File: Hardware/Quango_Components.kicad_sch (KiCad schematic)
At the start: 112 parts, among them J1 Conn_01x12_Male, J2 Conn_01x12_Male, J3 Conn_01x12_Male, J4 Conn_01x12_Male, J5 SWD_Header, J6 Eurorack_10_pin_power, Q1 MMBT3904, U1 LM1117-3.3, U2 STM32G473V, U3 LM1117-5.0, U4 PS508, U5 MCP6002, U6 AS3364, U7 AS3364, U8 AD5676, U9 MCP48CMB21, Y1 8MHz 20pF

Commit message: Added Test Points
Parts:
- added TP1, TP2, TP3, TP4, TP5, TP6, TP7: TestPoint, Connector_PinSocket_2.54mm:PinSocket_1x01_P2.54mm_Vertical, symbol Connector:TestPoint
- D2, D3: symbol Diode:1N5819 -> Device:D_Schottky_Small
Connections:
- net +12V: now also TP1.1
- net +3.3V: now also TP5.1
- net +5V: now also TP3.1
- net -12V: now also TP2.1
- net -5V_REF: now also TP4.1
- net GND: now also TP6.1, TP7.1
- no-connect marks 37 -> 38
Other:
- moved on the sheet: C29, C33, J1, J2, J3, J4, J5, R20, R24, R28, R32, RESET1

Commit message: First draft routing of control board
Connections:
- net EnvA1_LED: now also R80.2, U2.1 (PE2); no longer R76.2, U2.59 (PD12)
- net EnvA1_LED_Out: now also J3.5 (Pin_5), R80.1; no longer J3.8 (Pin_8), R76.1
- net EnvA2_LED: now also R81.2, U2.2 (PE3); no longer R77.2, U2.60 (PD13)
- net EnvA2_LED_Out: now also J3.4 (Pin_4), R81.1; no longer J3.7 (Pin_7), R77.1
- net EnvA3_LED: now also R82.2, U2.3 (PE4); no longer R78.2, U2.61 (PD14)
- net EnvA3_LED_Out: now also J3.3 (Pin_3), R82.1; no longer J3.9 (Pin_9), R78.1
- net EnvA4_LED: now also R83.2, U2.4 (PE5); no longer R79.2, U2.96 (PB9)
- net EnvA4_LED_Out: now also J3.2 (Pin_2), R83.1; no longer J3.6 (Pin_6), R79.1
- net EnvB1_LED: now also R76.2, U2.59 (PD12); no longer R80.2, U2.1 (PE2)
- net EnvB1_LED_Out: now also J3.8 (Pin_8), R76.1; no longer J3.5 (Pin_5), R80.1
- net EnvB2_LED: now also R77.2, U2.60 (PD13); no longer R81.2, U2.2 (PE3)
- net EnvB2_LED_Out: now also J3.7 (Pin_7), R77.1; no longer J3.4 (Pin_4), R81.1
- net EnvB3_LED: now also R78.2, U2.61 (PD14); no longer R82.2, U2.3 (PE4)
- net EnvB3_LED_Out: now also J3.9 (Pin_9), R78.1; no longer J3.3 (Pin_3), R82.1
- net EnvB4_LED: now also R79.2, U2.96 (PB9); no longer R83.2, U2.4 (PE5)
- net EnvB4_LED_Out: now also J3.6 (Pin_6), R79.1; no longer J3.2 (Pin_2), R83.1
- net USB_DM: now also J4.1 (Pin_1); no longer J4.2 (Pin_2)
- net USB_DP: now also J4.2 (Pin_2); no longer J4.1 (Pin_1)
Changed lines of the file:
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@@
     (effects (font (size 1.27 1.27)) (justify left bottom))
   )
-  (label "USB_DP" (at -35.56 50.8 0)
+  (label "USB_DP" (at -35.56 53.34 0)
     (effects (font (size 1.27 1.27)) (justify left bottom))
   )
@@
     (effects (font (size 1.27 1.27)) (justify right bottom))
   )
-  (label "EnvA2_LED_Out" (at 360.68 160.02 0)
+  (label "EnvA2_LED_Out" (at 360.68 180.34 0)
     (effects (font (size 1.27 1.27)) (justify left bottom))
   )
@@
     (effects (font (size 1.27 1.27)) (justify right bottom))
   )
-  (label "EnvB2_LED_Out" (at 360.68 180.34 0)
+  (label "EnvB2_LED_Out" (at 360.68 160.02 0)
     (effects (font (size 1.27 1.27)) (justify left bottom))
   )
@@
     (effects (font (size 1.27 1.27)) (justify left bottom))
   )
-  (label "EnvA3_LED_Out" (at -39.37 30.48 0)
+  (label "EnvA3_LED_Out" (at -39.37 15.24 0)
     (effects (font (size 1.27 1.27)) (justify left bottom))
   )
@@
     (effects (font (size 1.27 1.27)) (justify right bottom))
   )
-  (label "EnvB4_LED_Out" (at 360.68 190.5 0)
+  (label "EnvB4_LED_Out" (at 360.68 170.18 0)
     (effects (font (size 1.27 1.27)) (justify left bottom))
   )
@@
     (effects (font (size 1.27 1.27)) (justify right bottom))
   )
-  (label "EnvA3_LED" (at 53.34 165.1 180)
+  (label "EnvA3_LED" (at 53.34 96.52 180)
     (effects (font (size 1.27 1.27)) (justify right bottom))
   )
@@
     (effects (font (size 1.27 1.27)) (justify left bottom))
   )
-  (label "EnvA1_LED_Out" (at 360.68 154.94 0)
+  (label "EnvA1_LED_Out" (at 360.68 175.26 0)
     (effects (font (size 1.27 1.27)) (justify left bottom))
   )
@@
     (effects (font (size 1.27 1.27)) (justify left bottom))
   )
-  (label "EnvA2_LED" (at 53.34 162.56 180)
+  (label "EnvA2_LED" (at 53.34 93.98 180)
     (effects (font (size 1.27 1.27)) (justify right bottom))
   )
@@
     (effects (font (size 1.27 1.27)) (justify right bottom))
   )
-  (label "EnvB4_LED_Out" (at -39.37 12.7 0)
+  (label "EnvB4_LED_Out" (at -39.37 22.86 0)
     (effects (font (size 1.27 1.27)) (justify left bottom))
   )
@@
     (effects (font (size 1.27 1.27)) (justify left bottom))
   )
-  (label "EnvB1_LED_Out" (at 360.68 175.26 0)
+  (label "EnvB1_LED_Out" (at 360.68 154.94 0)
     (effects (font (size 1.27 1.27)) (justify left bottom))
   )
@@
     (effects (font (size 1.27 1.27)) (justify right bottom))
   )
-  (label "EnvA4_LED" (at 353.06 170.18 180)
+  (label "EnvA4_LED" (at 353.06 190.5 180)
     (effects (font (size 1.27 1.27)) (justify right bottom))
   )
@@
     (effects (font (size 1.27 1.27)) (justify right bottom))
   )
-  (label "USB_DM" (at -35.56 53.34 0)
+  (label "USB_DM" (at -35.56 50.8 0)
     (effects (font (size 1.27 1.27)) (justify left bottom))
   )
@@
     (effects (font (size 1.27 1.27)) (justify left bottom))
   )
-  (label "EnvB3_LED" (at 353.06 185.42 180)
+  (label "EnvB3_LED" (at 353.06 165.1 180)
     (effects (font (size 1.27 1.27)) (justify right bottom))
   )
@@
     (effects (font (size 1.27 1.27)) (justify left bottom))
   )
-  (label "EnvB2_LED_Out" (at -39.37 17.78 0)
+  (label "EnvB2_LED_Out" (at -39.37 25.4 0)
     (effects (font (size 1.27 1.27)) (justify left bottom))
   )
@@
     (effects (font (size 1.27 1.27)) (justify left bottom))
   )
-  (label "EnvB4_LED" (at 353.06 190.5 180)
+  (label "EnvB4_LED" (at 353.06 170.18 180)
     (effects (font (size 1.27 1.27)) (justify right bottom))
   )
@@
     (effects (font (size 1.27 1.27)) (justify left bottom))
   )
-  (label "EnvB3_LED_Out" (at 360.68 185.42 0)
-    (effects (font (size 1.27 1.27)) (justify left bottom))
-  )
-  (label "EnvB1_LED" (at 53.34 91.44 180)
+  (label "EnvB3_LED_Out" (at 360.68 165.1 0)
+    (effects (font (size 1.27 1.27)) (justify left bottom))
+  )
+  (label "EnvB1_LED" (at 53.34 160.02 180)
     (effects (font (size 1.27 1.27)) (justify right bottom))
   )
@@
     (effects (font (size 1.27 1.27)) (justify left bottom))
   )
-  (label "EnvB2_LED" (at 353.06 180.34 180)
+  (label "EnvB2_LED" (at 353.06 160.02 180)
     (effects (font (size 1.27 1.27)) (justify right bottom))
   )
@@
     (effects (font (size 1.27 1.27)) (justify right bottom))
   )
-  (label "EnvA3_LED_Out" (at 360.68 165.1 0)
-    (effects (font (size 1.27 1.27)) (justify left bottom))
-  )
-  (label "EnvB3_LED_Out" (at -39.37 15.24 0)
+  (label "EnvA3_LED_Out" (at 360.68 185.42 0)
+    (effects (font (size 1.27 1.27)) (justify left bottom))
+  )
+  (label "EnvB3_LED_Out" (at -39.37 30.48 0)
     (effects (font (size 1.27 1.27)) (justify left bottom))
   )
@@
     (effects (font (size 1.27 1.27)) (justify right bottom))
   )
-  (label "EnvB4_LED" (at 53.34 99.06 180)
-    (effects (font (size 1.27 1.27)) (justify right bottom))
-  )
-  (label "EnvB1_LED" (at 353.06 175.26 180)
-    (effects (font (size 1.27 1.27)) (justify right bottom))
-  )
-  (label "EnvA3_LED" (at 353.06 165.1 180)
+  (label "EnvB4_LED" (at 99.06 109.22 0)
+    (effects (font (size 1.27 1.27)) (justify left bottom))
+  )
+  (label "EnvB1_LED" (at 353.06 154.94 180)
+    (effects (font (size 1.27 1.27)) (justify right bottom))
+  )
+  (label "EnvA3_LED" (at 353.06 185.42 180)
     (effects (font (size 1.27 1.27)) (justify right bottom))
   )
@@
     (effects (font (size 1.27 1.27)) (justify right bottom))
   )
-  (label "EnvA1_LED_Out" (at -39.37 27.94 0)
+  (label "EnvA1_LED_Out" (at -39.37 20.32 0)
     (effects (font (size 1.27 1.27)) (justify left bottom))
   )
@@
     (effects (font (size 1.27 1.27)) (justify right bottom))
   )
-  (label "EnvB1_LED_Out" (at -39.37 20.32 0)
-    (effects (font (size 1.27 1.27)) (justify left bottom))
-  )
-  (label "EnvB3_LED" (at 53.34 96.52 180)
+  (label "EnvB1_LED_Out" (at -39.37 27.94 0)
+    (effects (font (size 1.27 1.27)) (justify left bottom))
+  )
+  (label "EnvB3_LED" (at 53.34 165.1 180)
     (effects (font (size 1.27 1.27)) (justify right bottom))
   )
@@
     (effects (font (size 1.27 1.27)) (justify right bottom))
   )
-  (label "EnvA1_LED" (at 353.06 154.94 180)
-    (effects (font (size 1.27 1.27)) (justify right bottom))
-  )
-  (label "EnvA2_LED" (at 353.06 160.02 180)
+  (label "EnvA1_LED" (at 353.06 175.26 180)
+    (effects (font (size 1.27 1.27)) (justify right bottom))
+  )
+  (label "EnvA2_LED" (at 353.06 180.34 180)
     (effects (font (size 1.27 1.27)) (justify right bottom))
   )
@@
     (effects (font (size 1.27 1.27)) (justify right bottom))
   )
-  (label "EnvA4_LED_Out" (at -39.37 22.86 0)
-    (effects (font (size 1.27 1.27)) (justify left bottom))
-  )
-  (label "EnvA4_LED" (at 99.06 109.22 0)
-    (effects (font (size 1.27 1.27)) (justify left bottom))
-  )
-  (label "EnvA2_LED_Out" (at -39.37 25.4 0)
+  (label "EnvA4_LED_Out" (at -39.37 12.7 0)
+    (effects (font (size 1.27 1.27)) (justify left bottom))
+  )
+  (label "EnvA4_LED" (at 53.34 99.06 180)
+    (effects (font (size 1.27 1.27)) (justify right bottom))
+  )
+  (label "EnvA2_LED_Out" (at -39.37 17.78 0)
     (effects (font (size 1.27 1.27)) (justify left bottom))
   )
@@
     (effects (font (size 1.27 1.27)) (justify right bottom))
   )
-  (label "EnvA4_LED_Out" (at 360.68 170.18 0)
+  (label "EnvA4_LED_Out" (at 360.68 190.5 0)
     (effects (font (size 1.27 1.27)) (justify left bottom))
   )
@@
     (effects (font (size 1.27 1.27)) (justify right bottom))
   )
-  (label "EnvA1_LED" (at 53.34 160.02 180)
+  (label "EnvA1_LED" (at 53.34 91.44 180)
     (effects (font (size 1.27 1.27)) (justify right bottom))
   )
@@
     (effects (font (size 1.27 1.27)) (justify right bottom))
   )
-  (label "EnvB2_LED" (at 53.34 93.98 180)
-    (effects (font (size 1.27 1.27)) (justify right bottom))
-  )
+  (label "EnvB2_LED" (at 53.34 162.56 180)
+    (effects (font (size 1.27 1.27)) (justify right bottom))
+  )

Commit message: Cleaned up Components schematic
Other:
- note added: "External DACs"
- note added: "LED resistors"
- note added: "MCU"
- note added: "MIDI/SWD"
- note added: "OpAmps"
- note added: "PItch Detection Multiplexer"
- note added: "Power"
- note removed: "Audio In for pitch detection"
- moved on the sheet: C1, C11, C12, C14, C17, C20, C21, C22, C23, C24, C25, C26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

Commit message: Schematic Clean Up
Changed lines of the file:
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@@
   )
   (text "DAC\n\nPA4 DAC1_OUT1\nPA5 DAC1_OUT2\n\nPA6 DAC2_OUT1\n\nPA2 DAC3_CH1\n[PB11 DAC3_CH1]\nPB1 DAC3_CH2\n\nPA8 DAC4_CH2\nPB12 DAC4_CH1\n"
-    (at -26.67 62.23 0)
+    (at -36.83 40.64 0)
     (effects (font (size 1.27 1.27)) (justify left bottom))
   )
@@
   )
   (text "PWM\n\nPD12 TIM4_CH1\nPD13 TIM4_CH2\nPD14 TIM4_CH3\nPD15 TIM4_CH4\n\nPE2 TIM3_CH1\nPE3 TIM3_CH2\nPE4 TIM3_CH3\nPE5 TIM3_CH4\n"
-    (at -26.67 214.63 0)
+    (at -36.83 193.04 0)
     (effects (font (size 1.27 1.27)) (justify left bottom))
   )
   (text "ADC\n\nPA0 ADC12_IN1\nPA1 ADC12_IN2\nPA2 ADC12_IN3\nPA3 ADC12_IN4\nPA4 ADC12_IN17\nPA5 ADC12_IN13\nPA6 ADC2_IN3\nPA7 ADC2_IN4\nPA8 ADC5_IN1\nPA9 ADC5_IN2\n\nPB0 ADC3_IN12/ADC1_IN15\nPB1 ADC3_IN1/ADC1_IN12\nPB2 ADC1_IN12\nPB11 ADC12_IN14\nPB12 ADC4_IN3/ADC1_IN11\nPB13 ADC3_IN5\nPB14 ADC4_IN4/ADC1_IN5\nPB15 ADC4_IN5/ADC2_IN15\n\nPC0 ADC12_IN6\nPC1 ADC12_IN7\nPC2 ADC12_IN8\nPC3 ADC12_IN9\nPC4 ADC2_IN5\nPC5 ADC2_IN11\n\nPD8 ADC4_IN12/ADC5_IN12\nPD9 ADC4_IN13/ADC5_IN13\nPD10 ADC345_IN7\nPD11 ADC345_IN8\nPD12 ADC345_IN9\nPD13 ADC345_IN10\nPD14 ADC345_IN11\n\nPE7 ADC3_IN4\nPE8 ADC345_IN6\nPE9 ADC3_IN2\nPE10 ADC345_IN14\nPE11 ADC345_IN15\nPE12 ADC345_IN16\nPE13 ADC3_IN3\nPE14 ADC4_IN1\nPE15 ADC4_IN2\n\nPF0 ADC1_IN10\nPF1 ADC2_IN10"
-    (at -26.67 179.07 0)
+    (at -36.83 157.48 0)
     (effects (font (size 1.27 1.27)) (justify left bottom))
   )

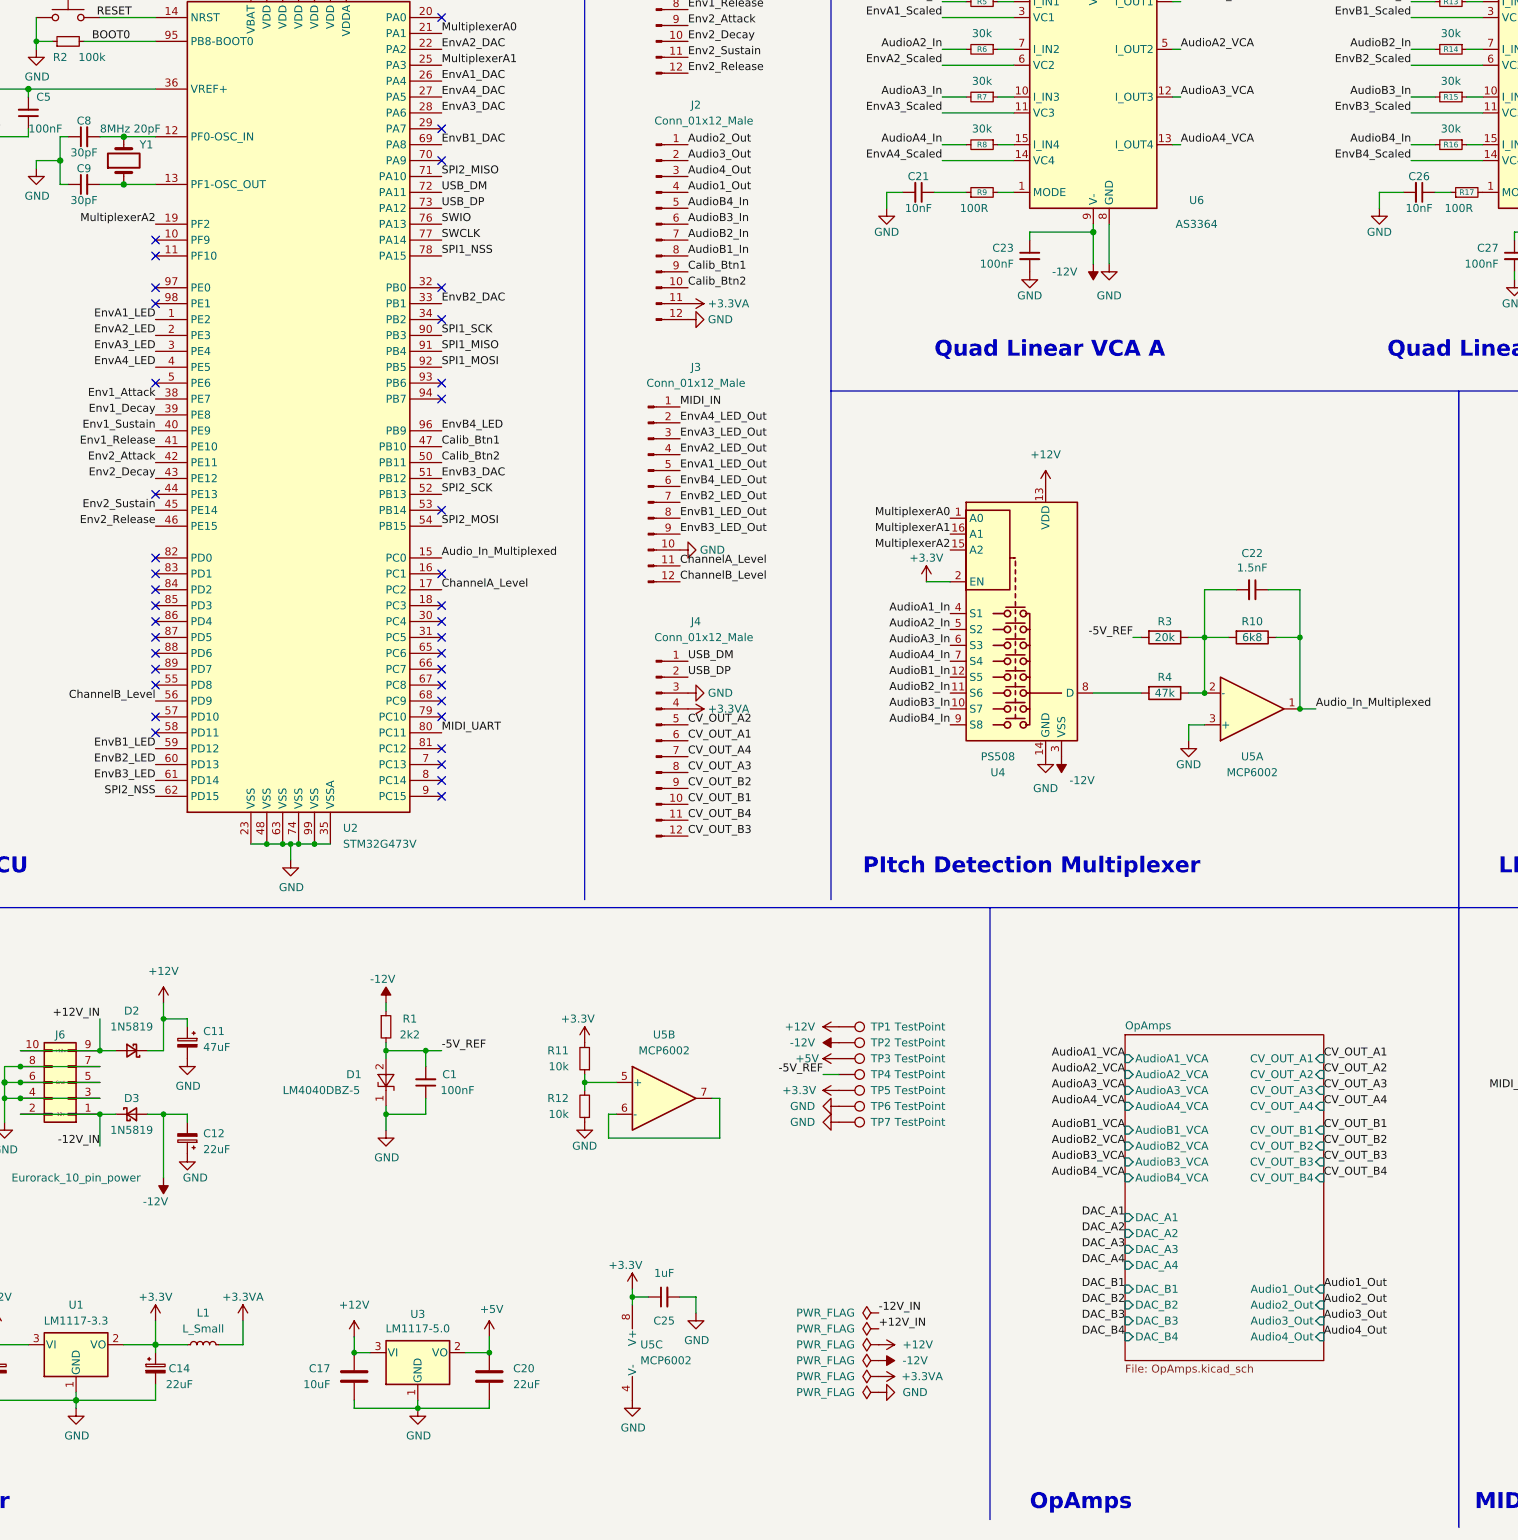
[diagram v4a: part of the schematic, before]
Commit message: Added Gate ouputs to component board
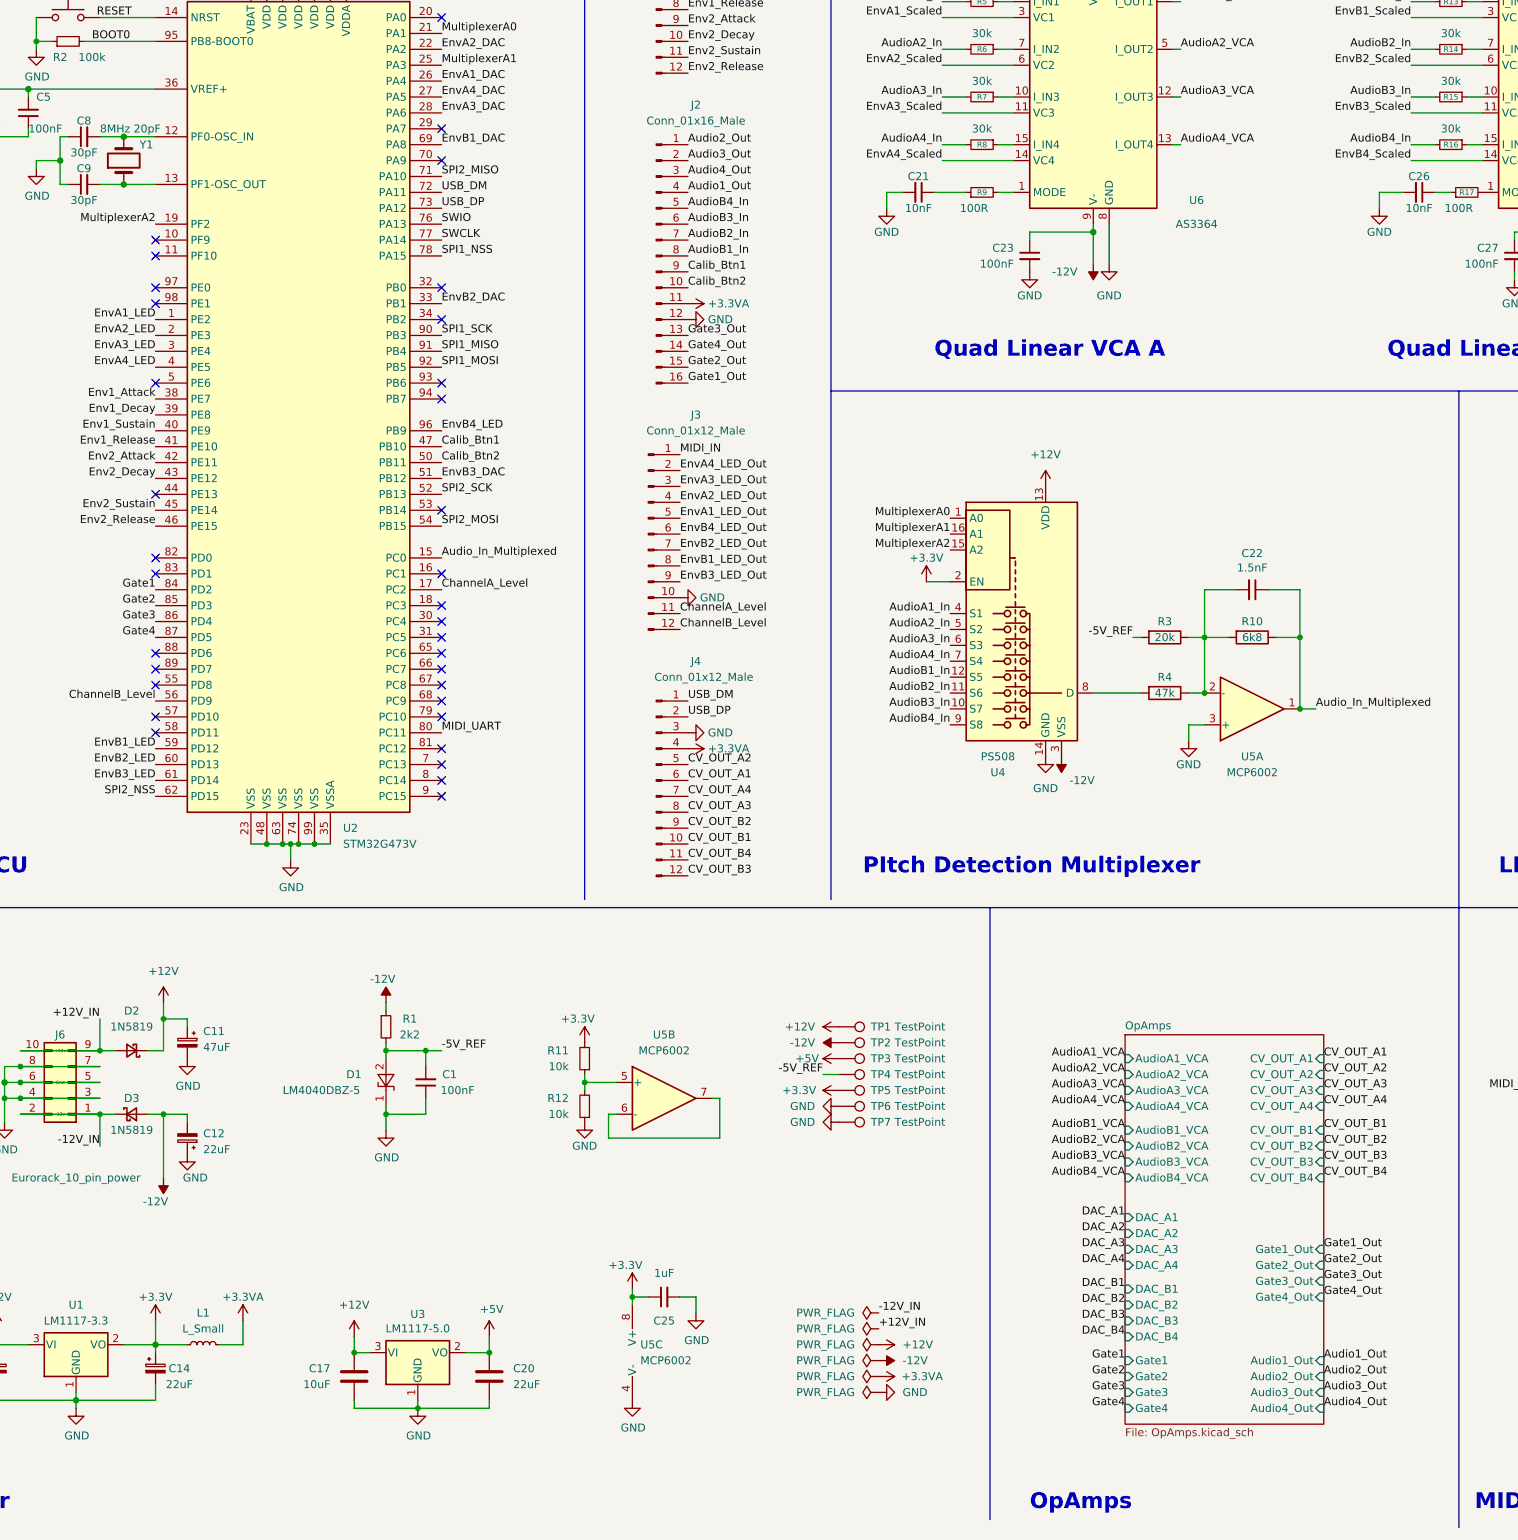
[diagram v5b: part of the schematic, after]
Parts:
- removed J2: Conn_01x12_Male, Connector_PinHeader_2.54mm:PinHeader_1x12_P2.54mm_Vertical, symbol Connector:Conn_01x12_Male
- added J2: Conn_01x16_Male, Connector_PinHeader_2.54mm:PinHeader_1x16_P2.54mm_Vertical, symbol Connector:Conn_01x16_Male
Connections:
- net +3.3VA: now also J2.11 (Pin_11)
- net Audio1_Out: now also J2.4 (Pin_4)
- net Audio2_Out: now also J2.1 (Pin_1)
- net Audio3_Out: now also J2.2 (Pin_2)
- net Audio4_Out: now also J2.3 (Pin_3)
- net AudioB1_In: now also J2.8 (Pin_8)
- net AudioB2_In: now also J2.7 (Pin_7)
- net AudioB3_In: now also J2.6 (Pin_6)
- net AudioB4_In: now also J2.5 (Pin_5)
- net Calib_Btn1: now also J2.9 (Pin_9)
- net Calib_Btn2: now also J2.10 (Pin_10)
- net GND: now also J2.12 (Pin_12)
- net Gate1: now reaches U2.84 (PD2)
- net Gate2: now reaches U2.85 (PD3)
- net Gate3: now reaches U2.86 (PD4)
- net Gate4: now reaches U2.87 (PD5)
- new net Gate1_Out: J2.16 (Pin_16)
- new net Gate2_Out: J2.15 (Pin_15)
- new net Gate3_Out: J2.13 (Pin_13)
- new net Gate4_Out: J2.14 (Pin_14)
- no-connect marks 38 -> 34
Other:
- sheet OpAmps ports: added Gate1, Gate1_Out, Gate2, Gate2_Out, Gate3, Gate3_Out, Gate4, Gate4_Out; removed none
- moved on the sheet: J3, J4
